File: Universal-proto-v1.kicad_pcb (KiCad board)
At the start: 2 copper layers, 81.5 x 121 mm, 44 parts, among them J1 Bus_ISA_8bit, J2 ISA Breakout, J3 Pico GPIO Breakout

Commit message: Lots of labels
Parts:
- moved U2 84.8 mm to (269.8, 21.9)
- moved U1 21.4 mm to (159.2, 68.2)
- moved J3 20.7 mm to (176.8, 46.6)
- moved JP1 19.1 mm to (109.7, 103.0)
- moved JP10 19.1 mm to (132.6, 103.0)
- moved JP11 19.1 mm to (135.1, 103.0)
- moved JP12 19.1 mm to (137.7, 103.0)
- moved JP13 19.1 mm to (140.2, 103.0)
- moved JP14 19.1 mm to (142.7, 103.0)
- moved JP15 19.1 mm to (145.3, 103.0)
- moved JP16 19.1 mm to (147.8, 103.0)
- moved JP17 19.1 mm to (150.4, 103.0)
- moved JP18 19.1 mm to (152.9, 103.0)
- moved JP19 19.1 mm to (155.5, 103.0)
- moved JP2 19.1 mm to (112.2, 103.0)
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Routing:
- net /GND: track 261.8 -> 12.5 mm, vias 5 -> 0
- net /GP35_ISA_RESET: track 145.5 -> 0.00 mm, vias 1 -> 0
- net /GP34_ISA_ALE: track 133.2 -> 0.00 mm
- net /GP33_ISA_CLK: track 112.1 -> 0.00 mm, vias 1 -> 0
- net /GP24_ISA_D4: track 111.9 -> 0.00 mm
- net /GP37: track 108.7 -> 0.00 mm, vias 1 -> 0
- net /GP22_ISA_D2: track 107.7 -> 0.00 mm
- net /GP36: track 108.5 -> 1.96 mm, vias 1 -> 0
- net /GP38: track 106.4 -> 0.00 mm, vias 1 -> 0
- net /GP39: track 105.6 -> 0.00 mm, vias 1 -> 0
- net /GP25_ISA_D5: track 104.1 -> 0.00 mm
- net /GP40: track 103.3 -> 0.00 mm, vias 1 -> 0
- net /GP41: track 102.6 -> 0.00 mm, vias 1 -> 0
- net /GP20_ISA_D0: track 102.8 -> 1.09 mm
- net /GP43: track 100.3 -> 0.00 mm, vias 1 -> 0
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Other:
- board text added: "+12V"
- board text added: "-12V"
- board text added: "-5V"
- board text added: "/DACK0"
- board text added: "/DACK1"
- board text added: "/DACK2"
- board text added: "/DACK3"
- board text added: "/IOR"
- board text added: "/IOW"
- board text added: "/SMEMR"
- board text added: "/SMEMW"
- board text added: "AEN"
- board text added: "ALE"
- board text added: "BA00"
- board text added: "BA01"
- board text added: "BA02"
- board text added: "BA03"
- board text added: "BA04"
- board text added: "BA05"
- board text added: "BA06"
- board text added: "BA07"
- board text added: "BA08"
- board text added: "BA09"
- board text added: "BA10"
- board text added: "BA11"
- board text added: "BA12"
- board text added: "BA13"
- board text added: "BA14"
- board text added: "BA15"
- board text added: "BA16"
- board text added: "BA17"
- board text added: "BA18"
- board text added: "BA19"
- board text added: "CLK"
- board text added: "DB0"
- board text added: "DB1"
- board text added: "DB2"
- board text added: "DB3"
- board text added: "DB4"
- board text added: "DB5"
- board text added: "DB6"
- board text added: "DB7"
- board text added: "DRQ1"
- board text added: "DRQ2"
- board text added: "DRQ3"
- board text added: "GP16_ISA_A15"
- board text added: "GP16_ISA_A16"
- board text added: "GP18_ISA_A18"
- board text added: "GP5_ISA_D5"
- board text added: "GP8_ISA_A8"
- board text added: "IO"
- board text added: "IO_READY"
- board text added: "IRQ2"
- board text added: "IRQ3"
- board text added: "IRQ4"
- board text added: "IRQ5"
- board text added: "IRQ6"
- board text added: "IRQ7"
- board text added: "OSC"
- board text added: "RESET"
- board text added: "TC"
- board text added: "UNUSED"
- board text added: "VCC"

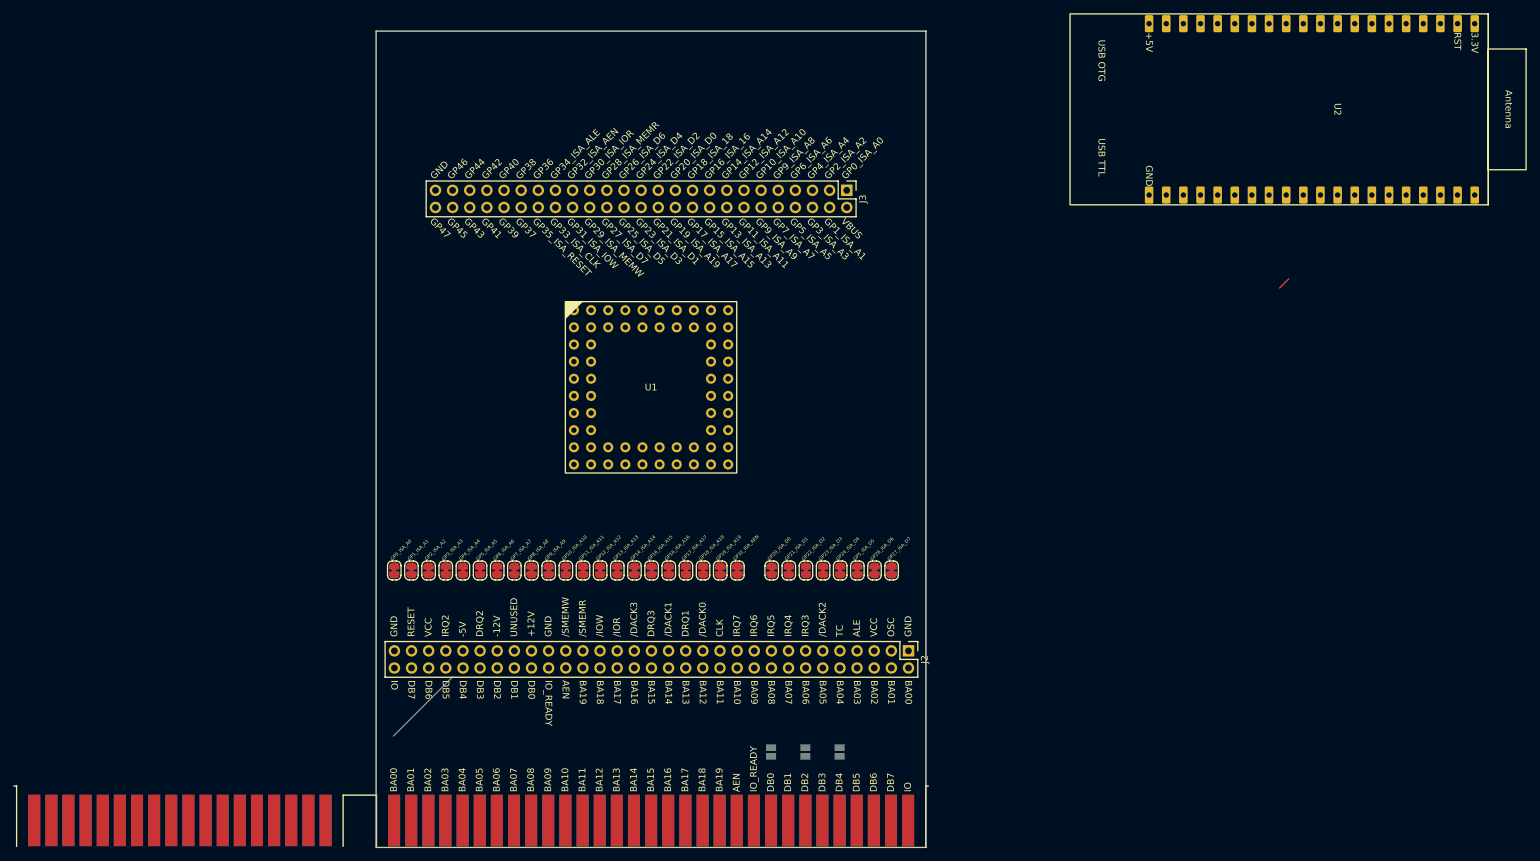
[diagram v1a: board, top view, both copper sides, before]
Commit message: Fix order of front labels
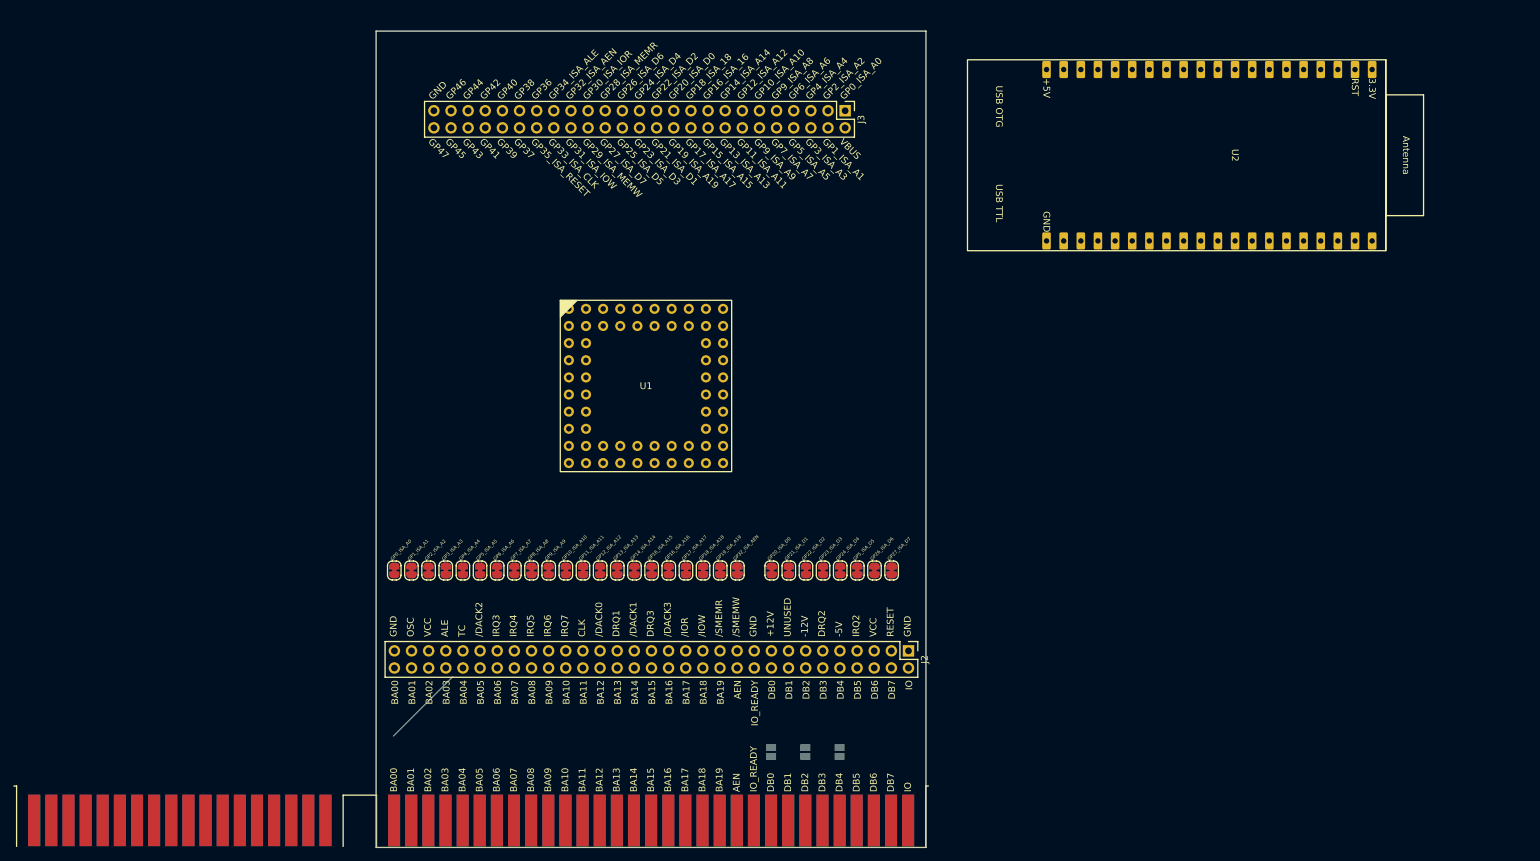
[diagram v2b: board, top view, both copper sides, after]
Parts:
- moved U2 16.7 mm to (254.6, 28.7)
- moved J3 11.8 mm to (176.5, 34.8)
- moved U1 0.78 mm to (158.4, 68.0)
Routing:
- net /GP36: track 1.96 -> 0.00 mm

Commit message: Pre-split of GPIO breakout
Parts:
- removed JP37, JP38, JP39: SolderJumper_2_Open, Jumper:SolderJumper-2_P1.3mm_Open_Pad1.0x1.5mm
- moved U2 69.7 mm to (184.9, 26.6)
- moved J3 58.2 mm to (118.5, 30.5), turned to 0 degrees
- moved U1 5.19 mm to (163.4, 69.4)
- moved J2 5.05 mm to (185.9, 119.9)
- moved JP1 5.05 mm to (109.7, 108.0)
- moved JP10 5.05 mm to (132.6, 108.0)
- moved JP11 5.05 mm to (135.1, 108.0)
- moved JP12 5.05 mm to (137.7, 108.0)
- moved JP13 5.05 mm to (140.2, 108.0)
- moved JP14 5.05 mm to (142.7, 108.0)
- moved JP15 5.05 mm to (145.3, 108.0)
- moved JP16 5.05 mm to (147.8, 108.0)
- moved JP17 5.05 mm to (150.4, 108.0)
- moved JP18 5.05 mm to (152.9, 108.0)
- moved JP19 5.05 mm to (155.5, 108.0)
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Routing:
- net /GND: track 12.5 -> 0.00 mm

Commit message: Everything seems to fit
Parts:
- added J4: Pico GPIO Breakout 1, Connector_PinHeader_2.54mm:PinHeader_2x13_P2.54mm_Vertical, F.Cu at (118.2, 61.6)
- added JP37: SolderJumper_2_Open, Jumper:SolderJumper-2_P1.3mm_Open_Pad1.0x1.5mm, B.Cu at (165.5, 134.2)
- added JP38: SolderJumper_2_Open, Jumper:SolderJumper-2_P1.3mm_Open_Pad1.0x1.5mm, B.Cu at (170.6, 134.2)
- added JP39: SolderJumper_2_Open, Jumper:SolderJumper-2_P1.3mm_Open_Pad1.0x1.5mm, B.Cu at (175.7, 134.2)
- J3: value Pico GPIO Breakout -> Pico GPIO Breakout 2; footprint Connector_PinHeader_2.54mm:PinHeader_2x25_P2.54mm_Vertical -> Connector_PinHeader_2.54mm:PinHeader_2x13_P2.54mm_Vertical
- moved J3 84.7 mm to (176.6, 92.1), turned to 180 degrees
- moved U1 5.29 mm to (158.1, 69.2)
- moved U2 5.16 mm to (179.8, 26.8)
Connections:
- J3 pad 1: /GP0_ISA_A0 -> /GP24_ISA_D4
- J3 pad 10: /GP7_ISA_A7 -> /GP31_ISA_IOW
- J3 pad 11: /GP10_ISA_A10 -> /GP34_ISA_ALE
- J3 pad 12: /GP9_ISA_A9 -> /GP33_ISA_CLK
- J3 pad 13: /GP12_ISA_A12 -> /GP36
- J3 pad 14: /GP11_ISA_A11 -> /GP35_ISA_RESET
- J3 pad 15: /GP14_ISA_A14 -> /GP38
- J3 pad 16: /GP13_ISA_A13 -> /GP37
- J3 pad 17: /GP16_ISA_A16 -> /GP40
- J3 pad 18: /GP15_ISA_A15 -> /GP39
- J3 pad 19: /GP18_ISA_A18 -> /GP42
- J3 pad 2: /VBUS -> /GND
- J3 pad 20: /GP17_ISA_A17 -> /GP41
- J3 pad 21: /GP20_ISA_D0 -> /GP44
- J3 pad 22: /GP19_ISA_A19 -> /GP43
- J3 pad 23: /GP22_ISA_D2 -> /GP46
- J3 pad 24: /GP21_ISA_D1 -> /GP45
- J3 pad 25: /GP24_ISA_D4 -> /VBUS
- J3 pad 26: /GP23_ISA_D3 -> /GP47
- J3 pad 3: /GP2_ISA_A2 -> /GP26_ISA_D6
- J3 pad 4: /GP1_ISA_A1 -> /GP25_ISA_D5
- J3 pad 5: /GP4_ISA_A4 -> /GP28_ISA_MEMR
- J3 pad 6: /GP3_ISA_A3 -> /GP27_ISA_D7
- J3 pad 7: /GP6_ISA_A6 -> /GP30_ISA_IOR
- J3 pad 8: /GP5_ISA_A5 -> /GP29_ISA_MEMW
- J3 pad 9: /GP8_ISA_A8 -> /GP32_ISA_AEN
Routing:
- net /GP11_ISA_A11: track 0.79 -> 0.00 mm
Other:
- board text removed: "GP16_ISA_16"
- board text removed: "GP9_ISA_A8"

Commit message: Fixups
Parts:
- moved J3 1.15 mm to (176.6, 93.2)
- moved J4 1.14 mm to (118.2, 62.8)
- moved U1 1.14 mm to (158.1, 70.4)
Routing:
- net /IRQ4: track 0.00 -> 21.1 mm
- net /IRQ5: track 0.00 -> 21.1 mm
- net /~{DACK2}: track 0.00 -> 21.1 mm
- net /GND: track 0.00 -> 21.1 mm
- net /VCC: track 0.00 -> 21.1 mm
- net /TC: track 0.00 -> 21.1 mm
- net /IRQ6: track 0.00 -> 21.1 mm
- net /OSC: track 0.00 -> 21.1 mm
- net /IRQ3: track 0.00 -> 21.1 mm
- net /ALE: track 0.00 -> 21.1 mm
- net /IRQ7: track 0.00 -> 21.1 mm
- net /CLK: track 0.00 -> 21.1 mm
- net /IO_READY: track 0.00 -> 17.6 mm
- net /DB7: track 0.00 -> 17.6 mm
- net /DB6: track 0.00 -> 17.6 mm
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
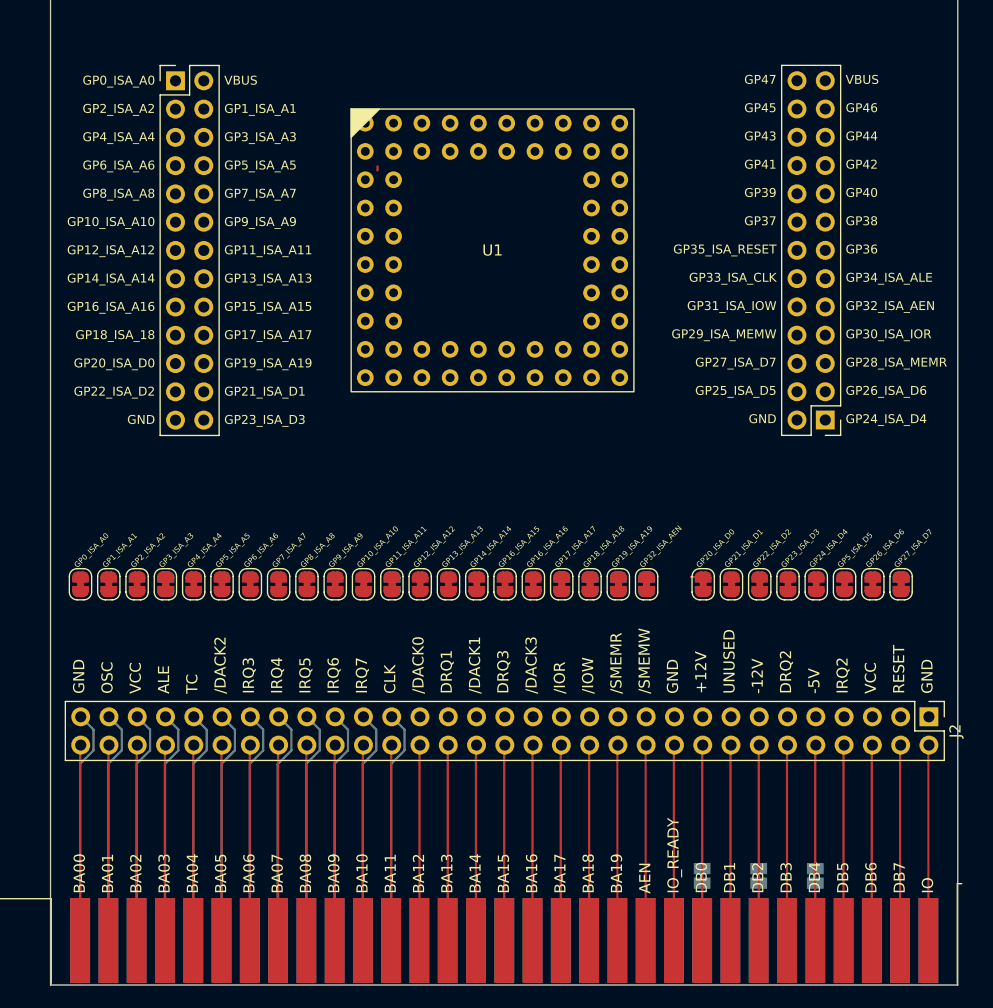
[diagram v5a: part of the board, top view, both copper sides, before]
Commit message: Core2350 connected to ISA bus
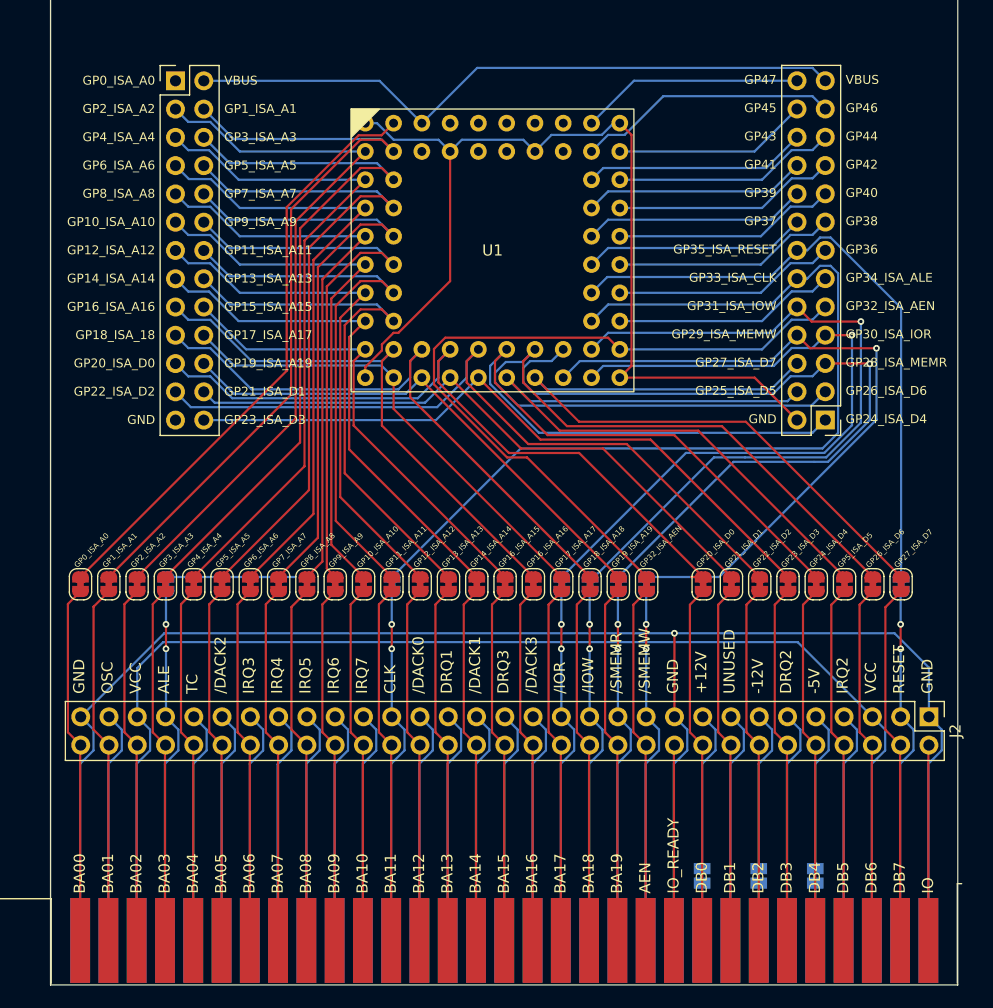
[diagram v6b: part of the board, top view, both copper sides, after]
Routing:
- net /GND: track 21.1 -> 246.5 mm, vias 0 -> 1
- net /VCC: track 21.1 -> 116.3 mm
- net /GP33_ISA_CLK: track 0.00 -> 84.2 mm
- net /GP26_ISA_D6: track 0.00 -> 78.4 mm
- net /GP24_ISA_D4: track 0.00 -> 75.6 mm
- net /GP28_ISA_MEMR: track 0.00 -> 71.8 mm, vias 0 -> 1
- net /GP1_ISA_A1: track 0.00 -> 70.7 mm
- net /GP22_ISA_D2: track 0.00 -> 67.8 mm
- net /GP32_ISA_AEN: track 0.00 -> 67.0 mm
- net /GP3_ISA_A3: track 0.01 -> 66.1 mm
- net /GP31_ISA_IOW: track 0.00 -> 65.5 mm, vias 0 -> 1
- net /GP2_ISA_A2: track 0.00 -> 65.4 mm
- net /GP27_ISA_D7: track 0.00 -> 65.3 mm
- net /GP25_ISA_D5: track 0.00 -> 65.1 mm
- net /GP30_ISA_IOR: track 0.00 -> 64.8 mm, vias 0 -> 1
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
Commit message: Everything connected
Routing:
- net /GND: track 246.5 -> 321.6 mm
- net /GP34_ISA_ALE: track 31.7 -> 72.3 mm
- net /GP24_ISA_D4: track 75.6 -> 53.3 mm, vias 0 -> 1
- net /GP0_ISA_A0: track 53.6 -> 74.8 mm

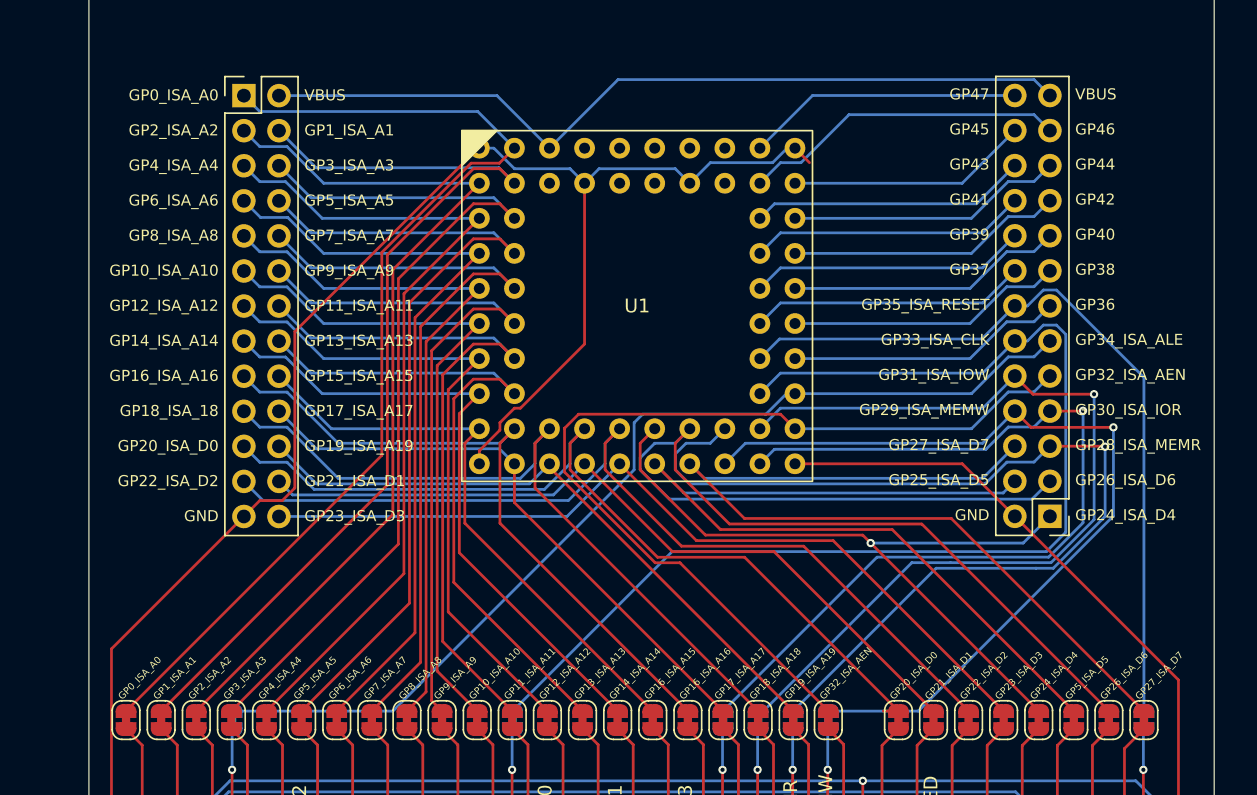
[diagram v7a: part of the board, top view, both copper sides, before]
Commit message: Fixed up text warnings
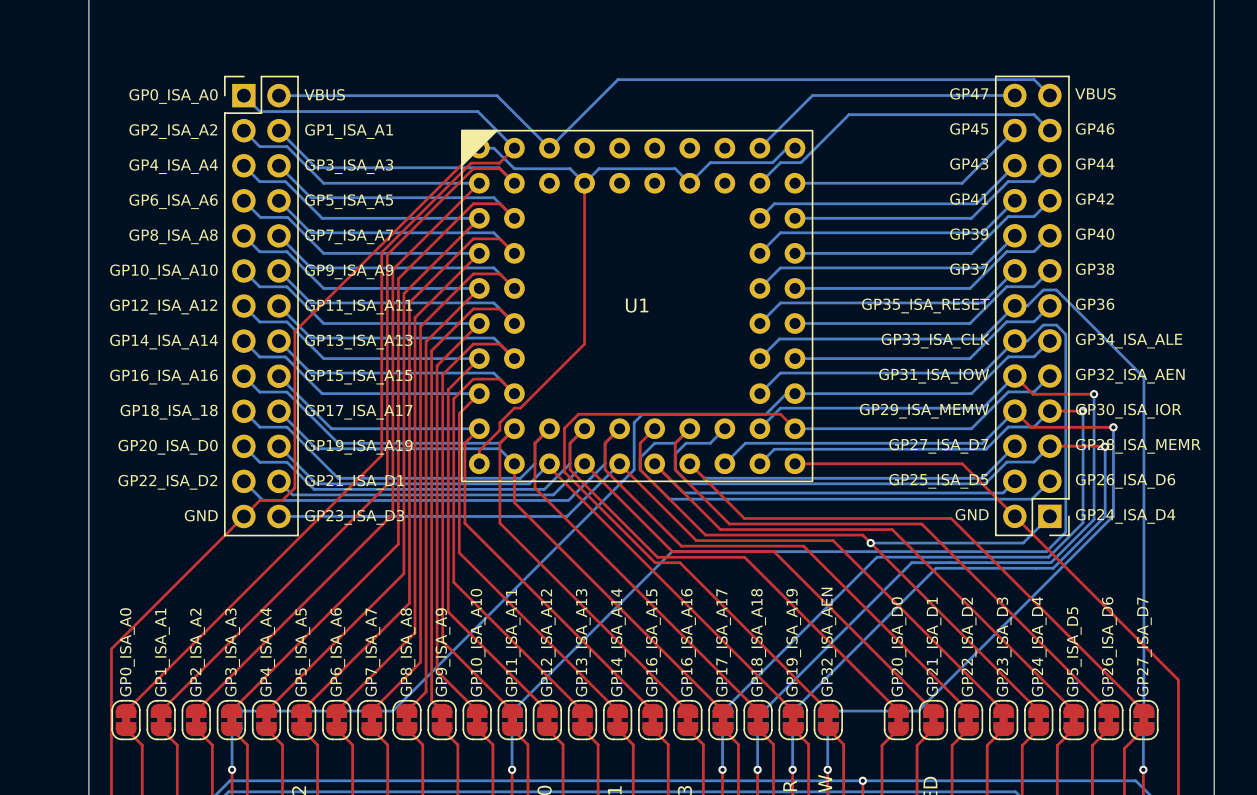
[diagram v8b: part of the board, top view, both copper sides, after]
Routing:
- net /GND: track 321.6 -> 320.2 mm
- net /GP20_ISA_D0: track 64.2 -> 63.1 mm
